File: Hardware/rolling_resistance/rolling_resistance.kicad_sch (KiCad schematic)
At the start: 14 parts, among them J1 JST-XH-3, J2 JST-XH-3, U1 LM339

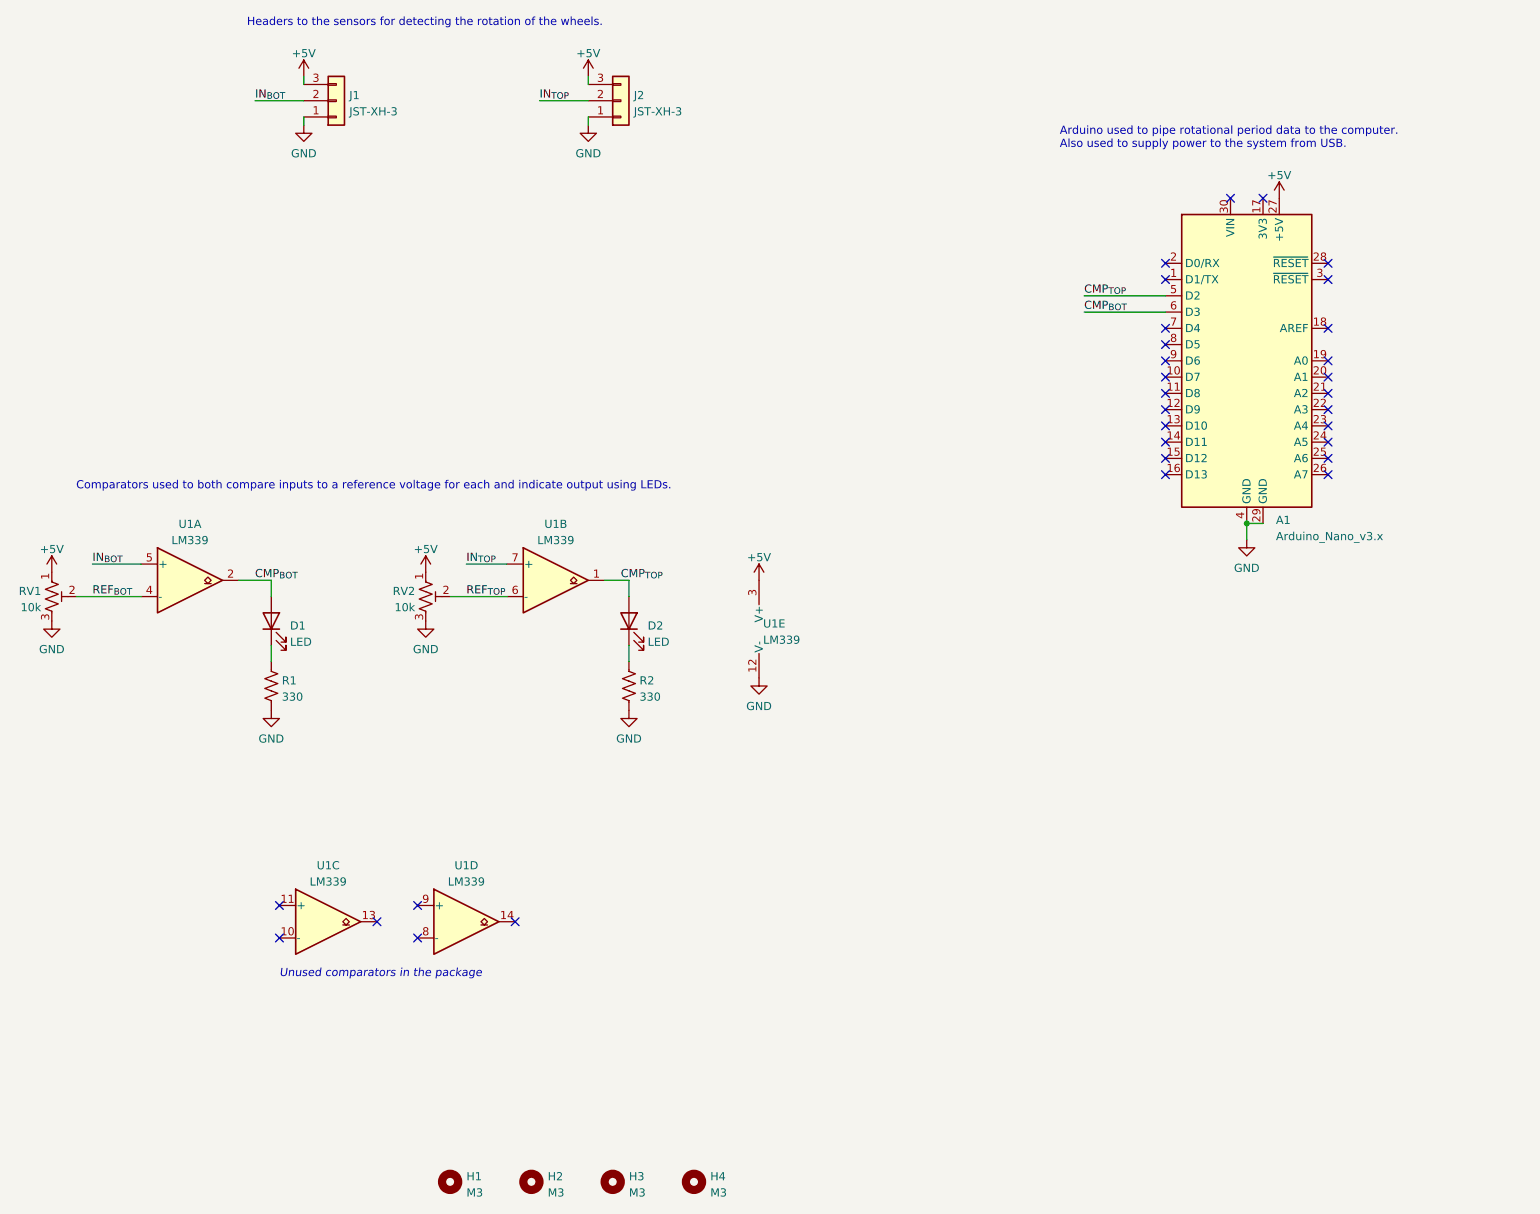
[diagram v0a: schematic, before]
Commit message: Updated hardware to what was ordered
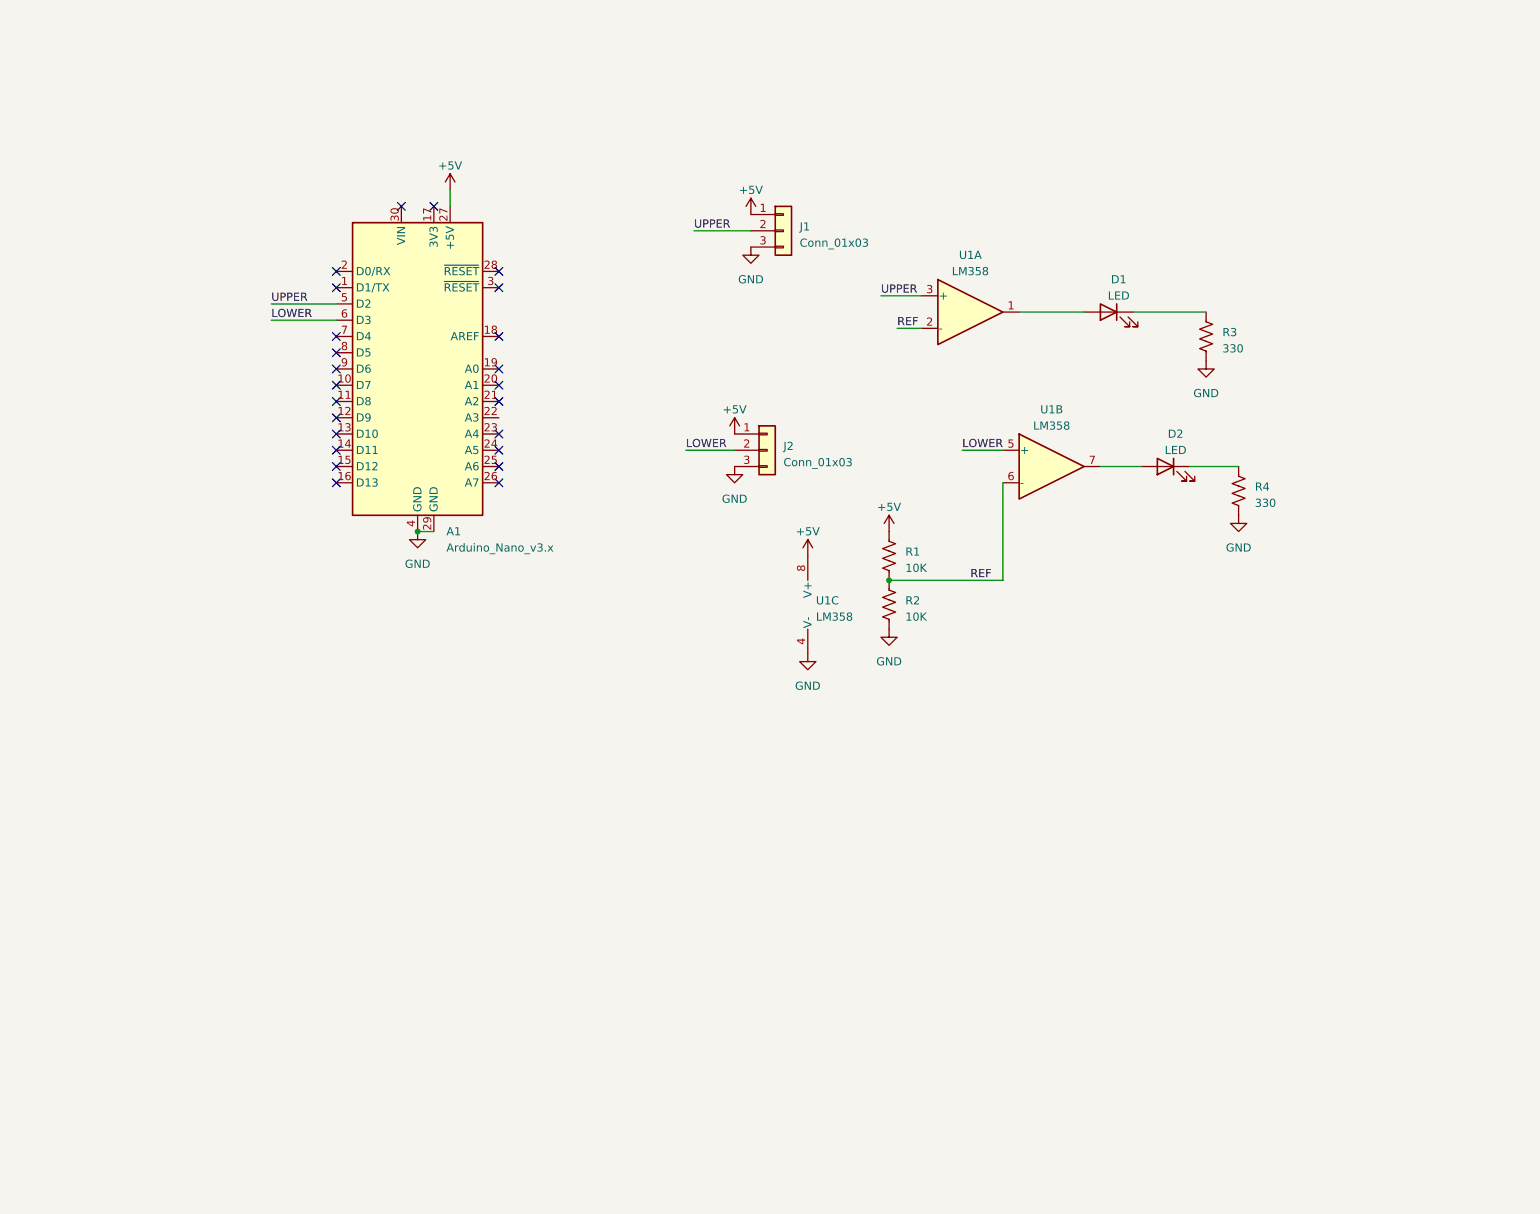
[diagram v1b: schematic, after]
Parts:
- removed H1, H2, H3, H4: M3, MountingHole:MountingHole_3.2mm_M3, symbol Mechanical:MountingHole
- removed RV1, RV2: 10k, Potentiometer_THT:Potentiometer_Bourns_3299W_Vertical, symbol Device:R_Potentiometer_Trim_US
- removed U1: LM339, Package_DIP:DIP-14_W7.62mm_LongPads, symbol Comparator:LM339
- added R3, R4: 330, Resistor_THT:R_Axial_DIN0207_L6.3mm_D2.5mm_P10.16mm_Horizontal, symbol Device:R_US
- added U1: LM358, Package_DIP:DIP-8_W7.62mm, symbol Amplifier_Operational:LM358
- D1, D2: footprint LED_THT:LED_D5.0mm -> LED_THT:LED_D4.0mm
- J1, J2: value JST-XH-3 -> Conn_01x03; footprint Connector_JST:JST_XH_B3B-XH-A_1x03_P2.50mm_Vertical -> Connector_JST:JST_EH_B3B-EH-A_1x03_P2.50mm_Vertical
- R1, R2: value 330 -> 10K; footprint Resistor_THT:R_Axial_DIN0207_L6.3mm_D2.5mm_P7.62mm_Horizontal -> Resistor_THT:R_Axial_DIN0207_L6.3mm_D2.5mm_P10.16mm_Horizontal
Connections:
- net +5V: now also J1.1 (Pin_1), J2.1 (Pin_1), R1.1, U1.8 (V+); no longer J1.3 (Pin_3), J2.3 (Pin_3)
- net GND: now also J1.3 (Pin_3), J2.3 (Pin_3), R3.2, R4.2, U1.4 (V-); no longer J1.1 (Pin_1), J2.1 (Pin_1), R1.2
- net at D1.1 (K): now also R3.1; no longer R1.1
- net at D2.1 (K): now also R4.1; no longer R2.1
- net CMP_{BOT}: no longer names the net of D1.2 (A)
- net CMP_{BOT}: now also U1.1; no longer A1.6 (D3)
- net CMP_{TOP}: no longer names the net of D2.2 (A)
- net CMP_{TOP}: now also U1.7; no longer A1.5 (D2)
- net IN_{BOT} renamed UPPER
- net UPPER: now also A1.5 (D2), U1.3 (+)
- net IN_{TOP} renamed LOWER
- net LOWER: now also A1.6 (D3), U1.5 (+)
- new net REF: R1.2, R2.1, U1.2 (-), U1.6 (-)
- no-connect marks 31 -> 24
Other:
- note removed: "Arduino used to pipe rotational period data to the computer. Also used to supply power to the system from USB."
- note removed: "Comparators used to both compare inputs to a reference voltage for each and indicate output using LEDs."
- note removed: "Headers to the sensors for detecting the rotation of the wheels."
- note removed: "Unused comparators in the package"
- title: Rolling Resistance Board -> Rolling Resistance Data Collector
